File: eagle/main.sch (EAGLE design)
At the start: 31 parts, among them IC1 7805TV, U1 INA213AIDCKT, U2 LM1117MP-3.3, U3 INA213AIDCKT, U4 INA213AIDCKT

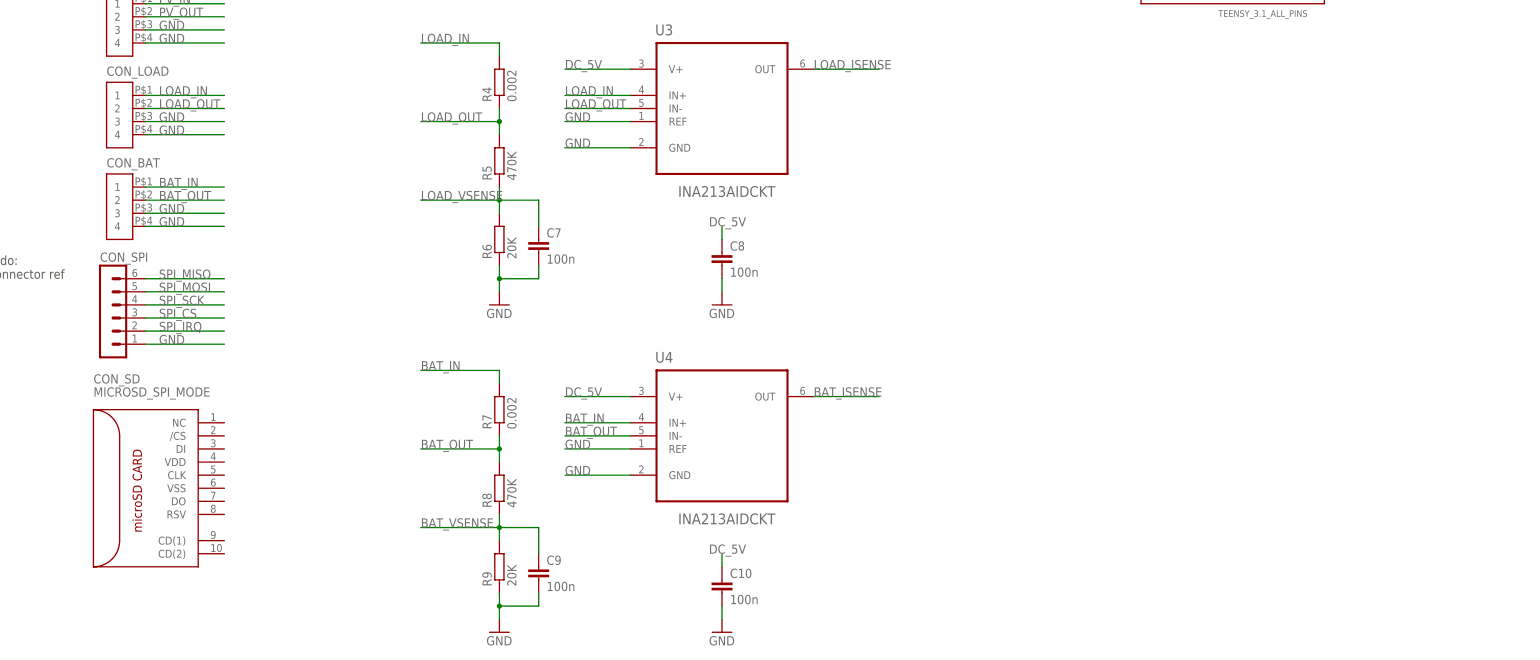
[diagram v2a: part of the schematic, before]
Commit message: add Spansion flash memory
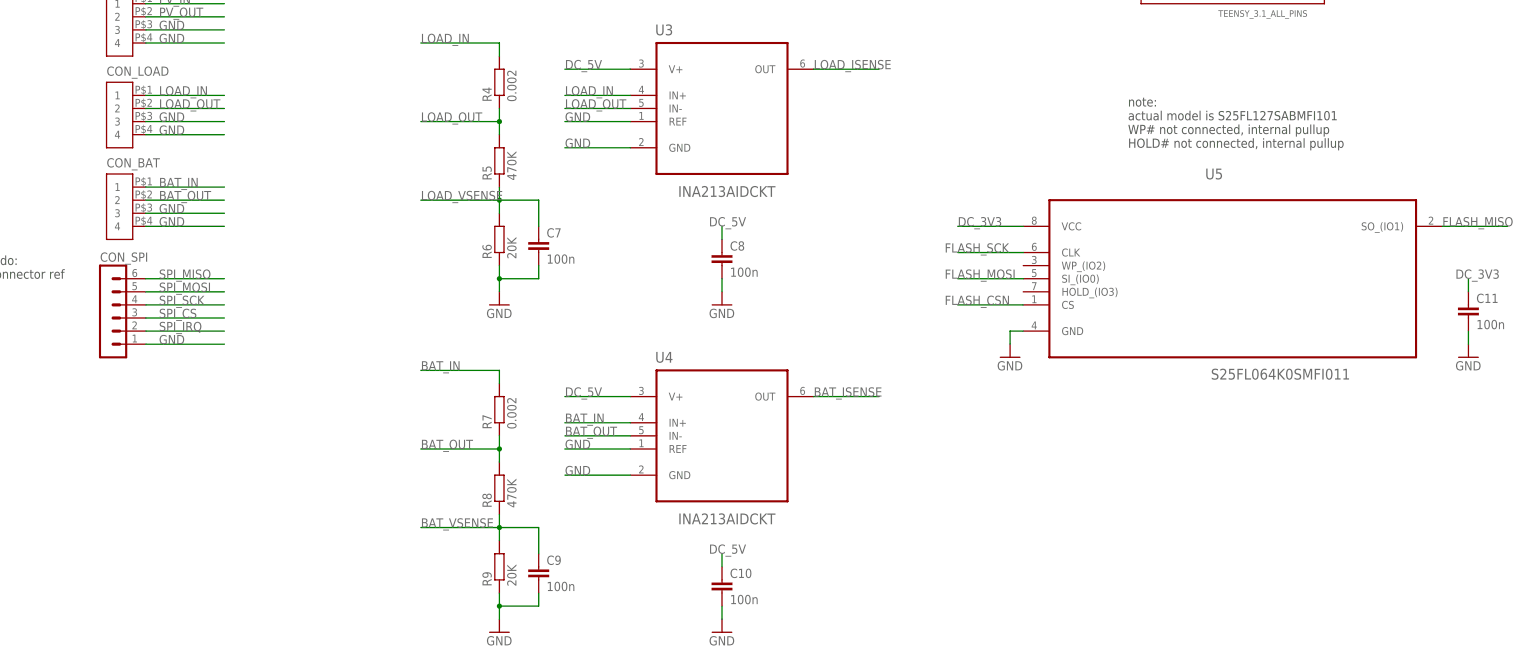
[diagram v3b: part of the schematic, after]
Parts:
- removed CON_SD: MICROSD_SPI_MODE, con-molex-microsd:MICROSD_SPI_MODE
- added C11: 100n, rcl:C-EUC1206
- added U5: S25FL064K0SMFI011, Spansion_By_element14_Batch_1:S25FL064K0SMFI011
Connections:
- new net FLASH_CSN: U5.CS
- new net FLASH_MISO: U5.SO_(IO1)
- new net FLASH_MOSI: U5.SI_(IO0)
- new net FLASH_SCK: U5.CLK
- net DC_3V3: now also C11.1, U5.VCC
- net GND: now also C11.2, U5.GND
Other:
- note added: "note: actual model is S25FL127SABMFI101 WP# not connected, internal pullup HOLD# not connected, internal pullup"
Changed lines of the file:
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@@
 <part name="C10" library="rcl" deviceset="C-EU" device="C1206" value="100n"/>
 <part name="GND12" library="supply1" deviceset="GND" device=""/>
-<part name="CON_SD" library="con-molex-microsd" deviceset="MICROSD_SPI_MODE" device=""/>
+<part name="U5" library="Spansion_By_element14_Batch_1" deviceset="S25FL064K0SMFI011" device=""/>
+<part name="GND13" library="supply1" deviceset="GND" device=""/>
+<part name="C11" library="rcl" deviceset="C-EU" device="C1206" value="100n"/>
+<part name="GND14" library="supply1" deviceset="GND" device=""/>
 </parts>
 <sheets>
@@
 disconnect the load and PV may
 not produce enough power</text>
+<text x="190.5" y="132.08" size="1.778" layer="97">note:
+actual model is S25FL127SABMFI101
+WP# not connected, internal pullup
+HOLD# not connected, internal pullup</text>
 </plain>
 <instances>
@@
 <instance part="C10" gate="G$1" x="111.76" y="48.26"/>
 <instance part="GND12" gate="1" x="111.76" y="38.1"/>
-<instance part="CON_SD" gate="G$1" x="2.54" y="66.04"/>
+<instance part="U5" gate="A" x="210.82" y="109.22"/>
+<instance part="GND13" gate="1" x="167.64" y="91.44"/>
+<instance part="C11" gate="G$1" x="256.54" y="101.6"/>
+<instance part="GND14" gate="1" x="256.54" y="91.44"/>
 </instances>
 <busses>
@@
 <wire x1="111.76" y1="43.18" x2="111.76" y2="40.64" width="0.1524" layer="91"/>
 <pinref part="GND12" gate="1" pin="GND"/>
+</segment>
+<segment>
+<pinref part="U5" gate="A" pin="GND"/>
+<wire x1="170.18" y1="96.52" x2="167.64" y2="96.52" width="0.1524" layer="91"/>
+<wire x1="167.64" y1="96.52" x2="167.64" y2="93.98" width="0.1524" layer="91"/>
+<pinref part="GND13" gate="1" pin="GND"/>
+</segment>
+<segment>
+<pinref part="C11" gate="G$1" pin="2"/>
+<wire x1="256.54" y1="96.52" x2="256.54" y2="93.98" width="0.1524" layer="91"/>
+<pinref part="GND14" gate="1" pin="GND"/>
 </segment>
 </net>
@@
 <junction x="139.7" y="251.46"/>
 </segment>
+<segment>
+<pinref part="U5" gate="A" pin="VCC"/>
+<wire x1="170.18" y1="116.84" x2="157.48" y2="116.84" width="0.1524" layer="91"/>
+<label x="157.48" y="116.84" size="1.778" layer="95"/>
+</segment>
+<segment>
+<pinref part="C11" gate="G$1" pin="1"/>
+<wire x1="256.54" y1="104.14" x2="256.54" y2="106.68" width="0.1524" layer="91"/>
+<label x="254" y="106.68" size="1.778" layer="95"/>
+</segment>
 </net>
 <net name="USB_5V" class="0">
@@
 </segment>
 </net>
+<net name="FLASH_SCK" class="0">
+<segment>
+<pinref part="U5" gate="A" pin="CLK"/>
+<wire x1="170.18" y1="111.76" x2="157.48" y2="111.76" width="0.1524" layer="91"/>
+<label x="154.94" y="111.76" size="1.778" layer="95"/>
+</segment>
+</net>
+<net name="FLASH_MOSI" class="0">
+<segment>
+<pinref part="U5" gate="A" pin="SI_(IO0)"/>
+<wire x1="170.18" y1="106.68" x2="157.48" y2="106.68" width="0.1524" layer="91"/>
+<label x="154.94" y="106.68" size="1.778" layer="95"/>
+</segment>
+</net>
+<net name="FLASH_CSN" class="0">
+<segment>
+<pinref part="U5" gate="A" pin="CS"/>
+<wire x1="170.18" y1="101.6" x2="157.48" y2="101.6" width="0.1524" layer="91"/>
+<label x="154.94" y="101.6" size="1.778" layer="95"/>
+</segment>
+</net>
+<net name="FLASH_MISO" class="0">
+<segment>
+<pinref part="U5" gate="A" pin="SO_(IO1)"/>
+<wire x1="251.46" y1="116.84" x2="264.16" y2="116.84" width="0.1524" layer="91"/>
+<label x="251.46" y="116.84" size="1.778" layer="95"/>
+</segment>
+</net>

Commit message: add dia
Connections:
- new net LOAD_GND: C7.2, CON_LOAD.3, CON_LOAD.4, R6.1
- new net PV_GND: C1.2, CON_PV.3, CON_PV.4, R3.1
- net GND: no longer C1.2, C7.2, CON_LOAD.3, CON_LOAD.4, CON_PV.3, CON_PV.4, R3.1, R6.1
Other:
- moved on the sheet: CON_SPI
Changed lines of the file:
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@@
 <part name="U2" library="NSC-LM1117MP-3.3" deviceset="LM1117MP-3.3" device=""/>
 <part name="CON_SPI" library="con-lstb" deviceset="MA06-1" device=""/>
-<part name="GND1" library="supply1" deviceset="GND" device=""/>
 <part name="C1" library="rcl" deviceset="C-EU" device="C1206" value="100n"/>
 <part name="C2" library="rcl" deviceset="C-EU" device="C1206" value="100n"/>
@@
 <part name="R5" library="rcl" deviceset="R-EU_" device="R0603" value="470K"/>
 <part name="R6" library="rcl" deviceset="R-EU_" device="R0603" value="20K"/>
-<part name="GND9" library="supply1" deviceset="GND" device=""/>
 <part name="C7" library="rcl" deviceset="C-EU" device="C1206" value="100n"/>
 <part name="C8" library="rcl" deviceset="C-EU" device="C1206" value="100n"/>
@@
 <part name="C11" library="rcl" deviceset="C-EU" device="C1206" value="100n"/>
 <part name="GND14" library="supply1" deviceset="GND" device=""/>
+<part name="GND1" library="supply1" deviceset="GND" device=""/>
 </parts>
 <sheets>
@@
 IN: from xxx, before shunt
 OUT: to xxx, after shunt</text>
-<text x="-30.48" y="106.68" size="1.778" layer="97">todo:
+<text x="-30.48" y="99.06" size="1.778" layer="97">todo:
 connector ref</text>
 <text x="20.32" y="271.78" size="1.778" layer="97">note:
@@
 <attribute name="VALUE" x="112.4712" y="238.7346" size="2.0828" layer="96" ratio="10" rot="SR0"/>
 </instance>
-<instance part="CON_SPI" gate="1" x="-7.62" y="101.6"/>
-<instance part="GND1" gate="1" x="68.58" y="165.1"/>
+<instance part="CON_SPI" gate="1" x="-7.62" y="93.98"/>
 <instance part="C1" gate="G$1" x="76.2" y="177.8"/>
 <instance part="C2" gate="G$1" x="111.76" y="175.26"/>
@@
 <instance part="R5" gate="G$1" x="68.58" y="129.54" rot="R90"/>
 <instance part="R6" gate="G$1" x="68.58" y="114.3" rot="R90"/>
-<instance part="GND9" gate="1" x="68.58" y="101.6"/>
 <instance part="C7" gate="G$1" x="76.2" y="114.3"/>
 <instance part="C8" gate="G$1" x="111.76" y="111.76"/>
@@
 <instance part="C11" gate="G$1" x="256.54" y="101.6"/>
 <instance part="GND14" gate="1" x="256.54" y="91.44"/>
+<instance part="GND1" gate="1" x="15.24" y="111.76"/>
 </instances>
 <busses>
@@
 <segment>
 <pinref part="CON_SPI" gate="1" pin="6"/>
-<wire x1="0" y1="106.68" x2="15.24" y2="106.68" width="0.1524" layer="91"/>
-<label x="2.54" y="106.68" size="1.778" layer="95"/>
-</segment>
-</net>
-<net name="SPI_MOSI" class="0">
-<segment>
-<pinref part="CON_SPI" gate="1" pin="5"/>
-<wire x1="0" y1="104.14" x2="15.24" y2="104.14" width="0.1524" layer="91"/>
-<label x="2.54" y="104.14" size="1.778" layer="95"/>
-</segment>
-</net>
-<net name="SPI_SCK" class="0">
-<segment>
-<pinref part="CON_SPI" gate="1" pin="4"/>
-<wire x1="0" y1="101.6" x2="15.24" y2="101.6" width="0.1524" layer="91"/>
-<label x="2.54" y="101.6" size="1.778" layer="95"/>
-</segment>
-</net>
-<net name="SPI_CS" class="0">
-<segment>
-<pinref part="CON_SPI" gate="1" pin="3"/>
 <wire x1="0" y1="99.06" x2="15.24" y2="99.06" width="0.1524" layer="91"/>
 <label x="2.54" y="99.06" size="1.778" layer="95"/>
 </segment>
 </net>
-<net name="SPI_IRQ" class="0">
-<segment>
-<pinref part="CON_SPI" gate="1" pin="2"/>
+<net name="SPI_MOSI" class="0">
+<segment>
+<pinref part="CON_SPI" gate="1" pin="5"/>
 <wire x1="0" y1="96.52" x2="15.24" y2="96.52" width="0.1524" layer="91"/>
 <label x="2.54" y="96.52" size="1.778" layer="95"/>
 </segment>
 </net>
-<net name="GND" class="0">
-<segment>
-<pinref part="CON_SPI" gate="1" pin="1"/>
+<net name="SPI_SCK" class="0">
+<segment>
+<pinref part="CON_SPI" gate="1" pin="4"/>
 <wire x1="0" y1="93.98" x2="15.24" y2="93.98" width="0.1524" layer="91"/>
 <label x="2.54" y="93.98" size="1.778" layer="95"/>
 </segment>
-<segment>
-<wire x1="0" y1="154.94" x2="15.24" y2="154.94" width="0.1524" layer="91"/>
-<label x="2.54" y="154.94" size="1.778" layer="95"/>
-<pinref part="CON_PV" gate="G$1" pin="3"/>
-</segment>
-<segment>
-<wire x1="0" y1="137.16" x2="15.24" y2="137.16" width="0.1524" layer="91"/>
-<label x="2.54" y="137.16" size="1.778" layer="95"/>
-<pinref part="CON_LOAD" gate="G$1" pin="3"/>
+</net>
+<net name="SPI_CS" class="0">
+<segment>
+<pinref part="CON_SPI" gate="1" pin="3"/>
+<wire x1="0" y1="91.44" x2="15.24" y2="91.44" width="0.1524" layer="91"/>
+<label x="2.54" y="91.44" size="1.778" layer="95"/>
+</segment>
+</net>
+<net name="SPI_IRQ" class="0">
+<segment>
+<pinref part="CON_SPI" gate="1" pin="2"/>
+<wire x1="0" y1="88.9" x2="15.24" y2="88.9" width="0.1524" layer="91"/>
+<label x="2.54" y="88.9" size="1.778" layer="95"/>
+</segment>
+</net>
+<net name="GND" class="0">
+<segment>
+<pinref part="CON_SPI" gate="1" pin="1"/>
+<wire x1="0" y1="86.36" x2="15.24" y2="86.36" width="0.1524" layer="91"/>
+<label x="2.54" y="86.36" size="1.778" layer="95"/>
 </segment>
 <segment>
@@
 <label x="2.54" y="119.38" size="1.778" layer="95"/>
 <pinref part="CON_BAT" gate="G$1" pin="3"/>
-</segment>
-<segment>
-<pinref part="R3" gate="G$1" pin="1"/>
+<wire x1="0" y1="116.84" x2="15.24" y2="116.84" width="0.1524" layer="91"/>
+<label x="2.54" y="116.84" size="1.778" layer="95"/>
+<pinref part="CON_BAT" gate="G$1" pin="4"/>
+<wire x1="15.24" y1="119.38" x2="15.24" y2="116.84" width="0.1524" layer="91"/>
+<wire x1="15.24" y1="116.84" x2="15.24" y2="114.3" width="0.1524" layer="91"/>
+<junction x="15.24" y="116.84"/>
 <pinref part="GND1" gate="1" pin="GND"/>
-<wire x1="68.58" y1="172.72" x2="68.58" y2="170.18" width="0.1524" layer="91"/>
-<pinref part="C1" gate="G$1" pin="2"/>
-<wire x1="68.58" y1="170.18" x2="68.58" y2="167.64" width="0.1524" layer="91"/>
-<wire x1="76.2" y1="172.72" x2="76.2" y2="170.18" width="0.1524" layer="91"/>
-<wire x1="76.2" y1="170.18" x2="68.58" y2="170.18" width="0.1524" layer="91"/>
-<junction x="68.58" y="170.18"/>
 </segment>
 <segment>
@@
 <wire x1="111.76" y1="170.18" x2="111.76" y2="167.64" width="0.1524" layer="91"/>
 <pinref part="GND2" gate="1" pin="GND"/>
-</segment>
-<segment>
-<wire x1="0" y1="152.4" x2="15.24" y2="152.4" width="0.1524" layer="91"/>
-<label x="2.54" y="152.4" size="1.778" layer="95"/>
-<pinref part="CON_PV" gate="G$1" pin="4"/>
-</segment>
-<segment>
-<wire x1="0" y1="134.62" x2="15.24" y2="134.62" width="0.1524" layer="91"/>
-<label x="2.54" y="134.62" size="1.778" layer="95"/>
-<pinref part="CON_LOAD" gate="G$1" pin="4"/>
-</segment>
-<segment>
-<wire x1="0" y1="116.84" x2="15.24" y2="116.84" width="0.1524" layer="91"/>
-<label x="2.54" y="116.84" size="1.778" layer="95"/>
-<pinref part="CON_BAT" gate="G$1" pin="4"/>
 </segment>
 <segment>
@@
 <wire x1="139.7" y1="241.3" x2="139.7" y2="238.76" width="0.1524" layer="91"/>
 <pinref part="GND8" gate="1" pin="GND"/>
-</segment>
-<segment>
-<pinref part="R6" gate="G$1" pin="1"/>
-<pinref part="GND9" gate="1" pin="GND"/>
-<wire x1="68.58" y1="109.22" x2="68.58" y2="106.68" width="0.1524" layer="91"/>
-<pinref part="C7" gate="G$1" pin="2"/>
-<wire x1="68.58" y1="106.68" x2="68.58" y2="104.14" width="0.1524" layer="91"/>
-<wire x1="76.2" y1="109.22" x2="76.2" y2="106.68" width="0.1524" layer="91"/>
-<wire x1="76.2" y1="106.68" x2="68.58" y2="106.68" width="0.1524" layer="91"/>
-<junction x="68.58" y="106.68"/>
 </segment>
 <segment>
@@
 </segment>
 </net>
+<net name="LOAD_GND" class="0">
+<segment>
+<wire x1="0" y1="137.16" x2="15.24" y2="137.16" width="0.1524" layer="91"/>
+<label x="2.54" y="137.16" size="1.778" layer="95"/>
+<pinref part="CON_LOAD" gate="G$1" pin="3"/>
+</segment>
+<segment>
+<wire x1="0" y1="134.62" x2="15.24" y2="134.62" width="0.1524" layer="91"/>
+<label x="2.54" y="134.62" size="1.778" layer="95"/>
+<pinref part="CON_LOAD" gate="G$1" pin="4"/>
+</segment>
+<segment>
+<pinref part="R6" gate="G$1" pin="1"/>
+<wire x1="68.58" y1="109.22" x2="68.58" y2="106.68" width="0.1524" layer="91"/>
+<pinref part="C7" gate="G$1" pin="2"/>
+<wire x1="76.2" y1="109.22" x2="76.2" y2="106.68" width="0.1524" layer="91"/>
+<wire x1="76.2" y1="106.68" x2="68.58" y2="106.68" width="0.1524" layer="91"/>
+<wire x1="68.58" y1="106.68" x2="53.34" y2="106.68" width="0.1524" layer="91"/>
+<junction x="68.58" y="106.68"/>
+<label x="53.34" y="106.68" size="1.778" layer="95"/>
+</segment>
+</net>
+<net name="PV_GND" class="0">
+<segment>
+<wire x1="0" y1="154.94" x2="15.24" y2="154.94" width="0.1524" layer="91"/>
+<label x="2.54" y="154.94" size="1.778" layer="95"/>
+<pinref part="CON_PV" gate="G$1" pin="3"/>
+</segment>
+<segment>
+<wire x1="0" y1="152.4" x2="15.24" y2="152.4" width="0.1524" layer="91"/>
+<label x="2.54" y="152.4" size="1.778" layer="95"/>
+<pinref part="CON_PV" gate="G$1" pin="4"/>
+</segment>
+<segment>
+<pinref part="R3" gate="G$1" pin="1"/>
+<wire x1="68.58" y1="172.72" x2="68.58" y2="170.18" width="0.1524" layer="91"/>
+<pinref part="C1" gate="G$1" pin="2"/>
+<wire x1="76.2" y1="172.72" x2="76.2" y2="170.18" width="0.1524" layer="91"/>
+<wire x1="76.2" y1="170.18" x2="68.58" y2="170.18" width="0.1524" layer="91"/>
+<junction x="68.58" y="170.18"/>
+<wire x1="68.58" y1="170.18" x2="53.34" y2="170.18" width="0.1524" layer="91"/>
+<label x="53.34" y="170.18" size="1.778" layer="95"/>
+</segment>
+</net>
